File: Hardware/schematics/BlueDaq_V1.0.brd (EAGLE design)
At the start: 100 x 80 mm, 66 parts, among them IC1 MEGA8-AI, Q1 MMBT2222, Q2 MMBT2222, Q3 MMBT2222, Q4 MMBT2222, U1 MCP73831, U2 TPS61200, U3 BME280, U4 MIC5225-3.3, U5 MIC5219 5V, X1 USB-MICROB, X2 3.5mm, X4 3.5mm, Y1 16 mhz

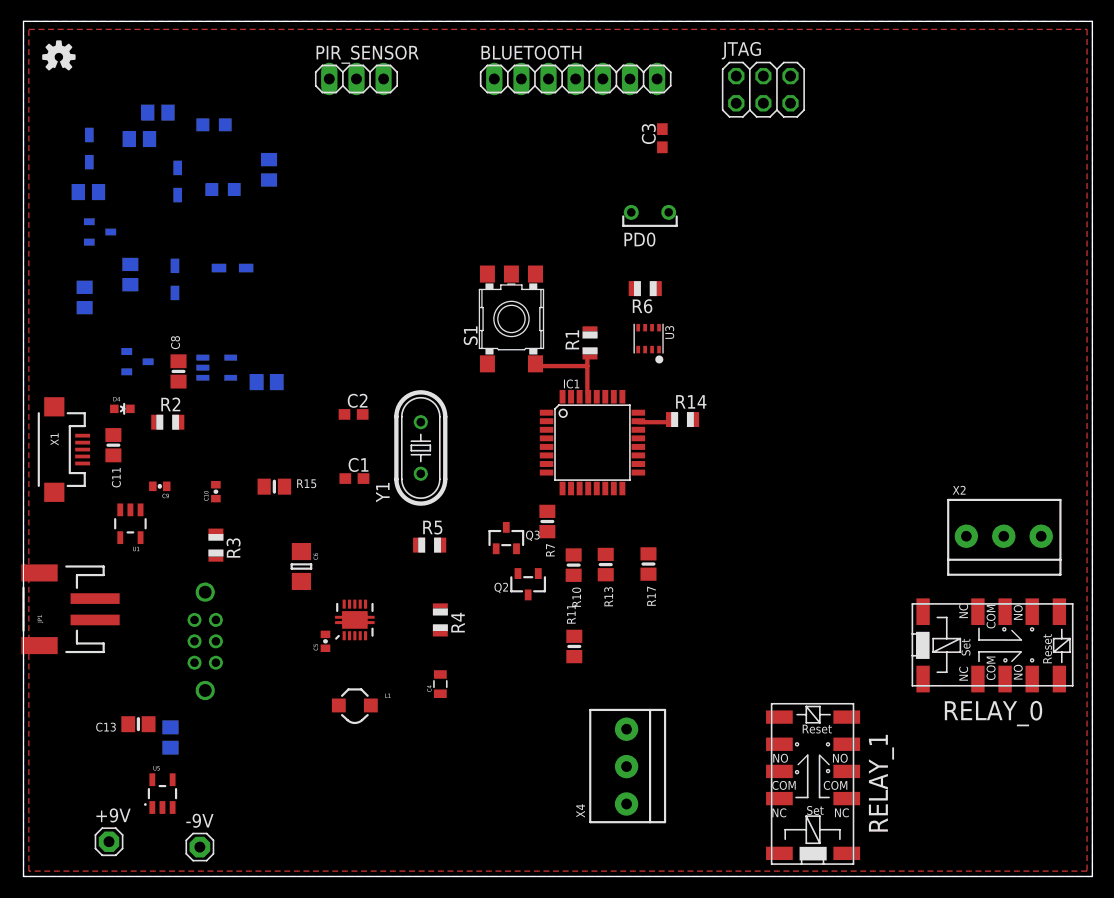
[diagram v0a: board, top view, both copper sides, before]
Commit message: updated board
updated layout. starting to have issue connecting gnd properly. added DRU/cam processor for OSH
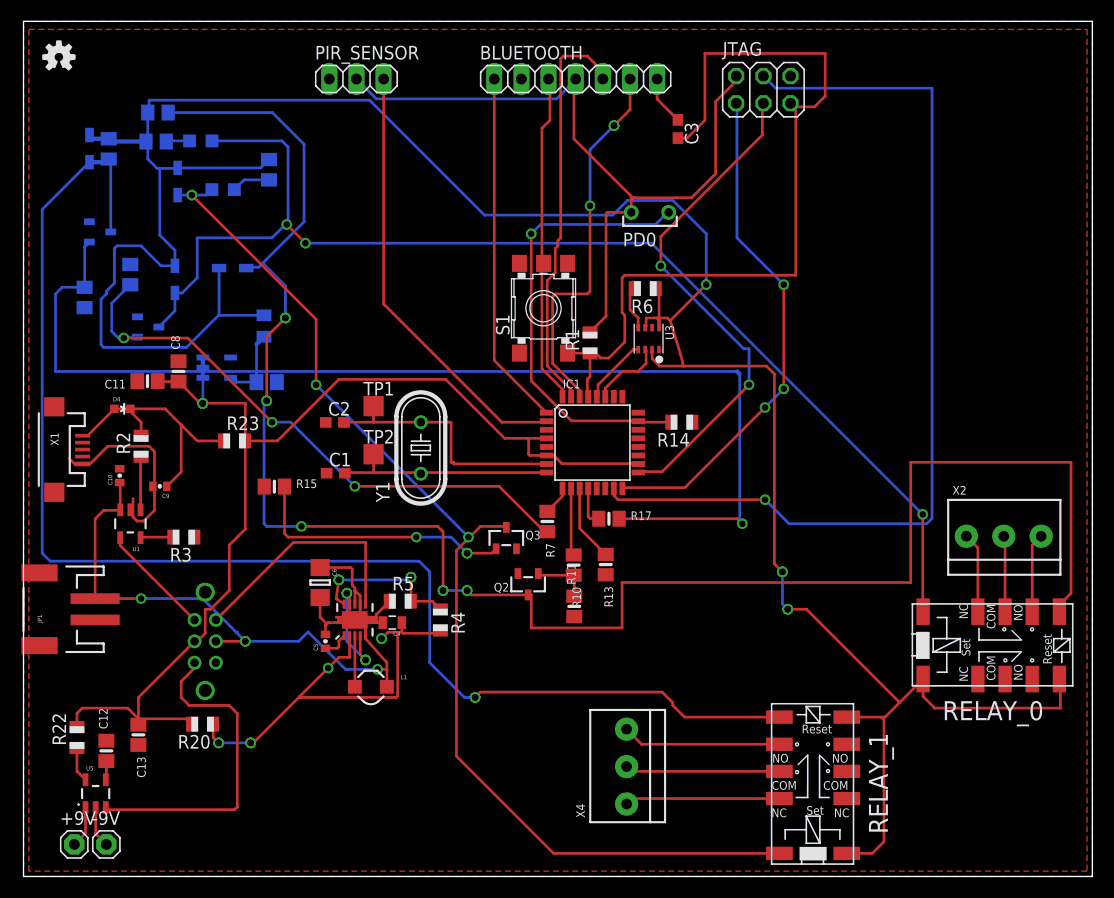
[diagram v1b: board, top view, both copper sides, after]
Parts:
- added R20, R21, R22, R23: 0, adafruit:R0805
- added TP1, TP2: TPTP19SQ, testpad:TP19SQ
- moved C10 9.12 mm to (9.00, 37.5)
- moved -9V 8.75 mm to (7.75, 3.00)
- moved C4 7.30 mm to (34.5, 23.8), turned to 180 degrees
- moved C11 6.79 mm to (11.6, 46.3), turned to 180 degrees
- moved U5 6.25 mm to (6.75, 7.75)
- moved C12 6.13 mm to (7.75, 11.8), flipped to the top
- moved R5 5.93 mm to (35.2, 25.8)
- moved R17 5.63 mm to (54.8, 33.5), turned to 0 degrees
- moved R19 4.46 mm to (7.97, 68.1), turned to 90 degrees
- moved R11 3.75 mm to (51.5, 25.3)
- moved Q1 3.40 mm to (11.7, 51.4)
- moved R2 3.36 mm to (11.0, 40.2), turned to 90 degrees
- moved +9V 3.26 mm to (4.75, 3.00)
- moved S1 3.16 mm to (48.6, 53.2)
- moved R3 3.09 mm to (15.0, 31.8), turned to 180 degrees
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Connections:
- new net N$20: C4.1, R20.1, R4.2, U2.2
- new net N$21: R22.1, U5.5
- new net N$23: C9.1, D4.A, R23.1, X1.VBUS
- new net OUT: C7.1, R21.1, U4.5
- net 3.3V: now also R21.2; no longer C7.1, U4.5
- net VCC: now also R20.2, R22.2, R23.2; no longer C4.1, C9.1, D4.A, R4.2, U2.2, U5.5, X1.VBUS
- net XTAL1: now also TP1.TP
- net XTAL2: now also TP2.TP
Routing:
- net 3.3V: track 0.00 -> 242.2 mm, vias 0 -> 3
- net VCC: track 0.00 -> 175.6 mm, vias 0 -> 2
- net N$25: track 0.00 -> 169.0 mm, vias 0 -> 5
- net N$12: track 0.00 -> 128.4 mm, vias 0 -> 1
- net N$6: track 0.00 -> 113.6 mm, vias 0 -> 3
- net N$7: track 0.00 -> 105.1 mm, vias 0 -> 3
- net N$13: track 0.00 -> 104.6 mm, vias 0 -> 1
- net SPI_MOSI: track 0.00 -> 88.2 mm, vias 0 -> 1
- net RESET_PIN: track 0.00 -> 77.7 mm
- net VBATT: track 0.00 -> 62.9 mm, vias 0 -> 3
- net N$22: track 0.00 -> 55.0 mm, vias 0 -> 3
- net SPI_SCK: track 0.00 -> 47.8 mm, vias 0 -> 2
- net SPI_MISO: track 0.00 -> 47.5 mm, vias 0 -> 3
- net N$1: track 0.00 -> 42.1 mm, vias 0 -> 1
- net N$20: track 0.00 -> 41.6 mm, vias 0 -> 4
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
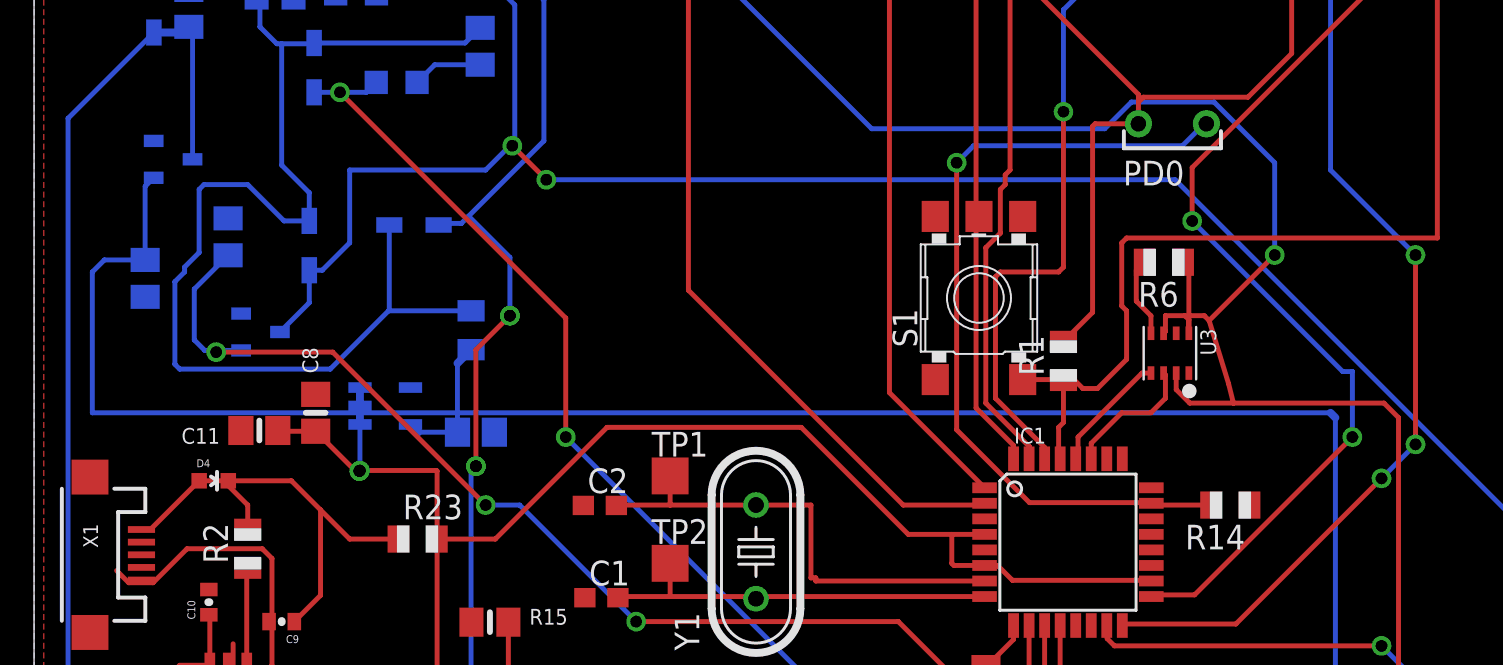
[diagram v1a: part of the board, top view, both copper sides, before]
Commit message: no more airwires, only need to clear DRC
everything is router now, for better or worse
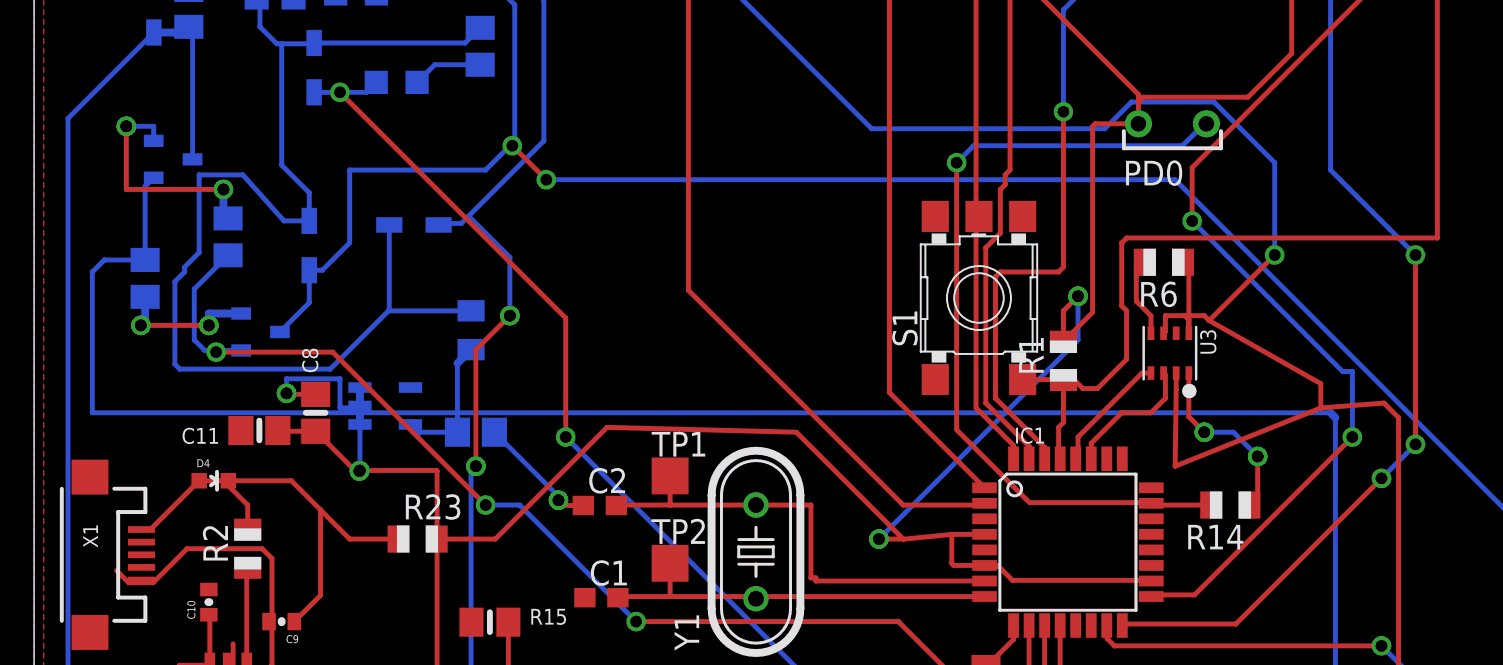
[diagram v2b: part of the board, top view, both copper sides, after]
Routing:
- net GND: track 19.0 -> 62.1 mm, vias 0 -> 8
- net VCC: track 175.6 -> 196.3 mm, vias 2 -> 4
- net 3.3V: track 242.2 -> 250.9 mm
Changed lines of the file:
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@@
 <?xml version="1.0" encoding="utf-8"?>
 <!DOCTYPE eagle SYSTEM "eagle.dtd">
-<eagle version="7.5.0">
+<eagle version="7.6.0">
 <drawing>
 <settings>
@@
 <wire x1="51.625" y1="74.5" x2="51.66" y2="74.61" width="0.254" layer="16"/>
 <wire x1="48.9374" y1="40.99" x2="47.25" y2="40.99" width="0.254" layer="1"/>
-<wire x1="47.25" y1="40.99" x2="45.01" y2="40.99" width="0.254" layer="1"/>
-<wire x1="45.01" y1="40.99" x2="39.5" y2="46.5" width="0.254" layer="1"/>
-<wire x1="39.5" y1="46.5" x2="29.5" y2="46.5" width="0.254" layer="1"/>
+<wire x1="47.25" y1="40.99" x2="44.76" y2="40.74" width="0.254" layer="1"/>
+<wire x1="44.75" y1="40.75" x2="39.25" y2="46.25" width="0.254" layer="1"/>
+<wire x1="39.25" y1="46.25" x2="29.5" y2="46.5" width="0.254" layer="1"/>
 <wire x1="29.5" y1="46.5" x2="23.75" y2="40.75" width="0.254" layer="1"/>
 <wire x1="23.75" y1="40.75" x2="20.75" y2="40.75" width="0.254" layer="1"/>
@@
 <wire x1="47.36" y1="39.39" x2="47.25" y2="39.5" width="0.254" layer="1"/>
 <wire x1="47.25" y1="39.5" x2="47.25" y2="40.99" width="0.254" layer="1"/>
-<wire x1="48.9374" y1="40.99" x2="53" y2="50.92" width="0" layer="19" extent="1-1"/>
+<wire x1="53" y1="50.92" x2="53" y2="52.5" width="0.254" layer="1"/>
+<wire x1="53" y1="52.5" x2="53.75" y2="53.25" width="0.254" layer="1"/>
+<via x="53.75" y="53.25" extent="1-16" drill="0.6"/>
+<wire x1="53.75" y1="53.25" x2="53.75" y2="51" width="0.254" layer="16"/>
+<wire x1="53.75" y1="51" x2="43.5" y2="40.75" width="0.254" layer="16"/>
+<via x="43.5" y="40.75" extent="1-16" drill="0.6"/>
+<wire x1="43.5" y1="40.75" x2="44.75" y2="40.75" width="0.254" layer="1"/>
+<wire x1="44.75" y1="40.75" x2="44.76" y2="40.74" width="0.254" layer="1"/>
 </signal>
 <signal name="GND">
@@
 <wire x1="9" y1="38.125" x2="9" y2="38.15" width="0.254" layer="1"/>
 <wire x1="9" y1="38.125" x2="9.00003125" y2="38.14998125" width="0.254" layer="1"/>
-<wire x1="14.5" y1="48.2" x2="16.7799" y2="47.6" width="0" layer="19" extent="1-16"/>
-<wire x1="9.99" y1="57.26" x2="6.16" y2="61.25" width="0" layer="19" extent="16-16"/>
-<wire x1="5.72" y1="53.22" x2="10.66" y2="52.36" width="0" layer="19" extent="16-16"/>
-<wire x1="28.28" y1="42.48" x2="23.7" y2="46.25" width="0" layer="19" extent="1-16"/>
-<wire x1="48.9374" y1="41.79" x2="46.4" y2="48.96" width="0" layer="19" extent="1-1"/>
-<wire x1="59.455" y1="49.295" x2="62.59" y2="42.5" width="0" layer="19" extent="1-1"/>
+<wire x1="9.99" y1="57.26" x2="9.75" y2="57.26" width="0.4064" layer="16"/>
+<wire x1="9.75" y1="57.26" x2="9.75" y2="58.75" width="0.4064" layer="16"/>
+<via x="9.75" y="58.75" extent="1-16" drill="0.6"/>
+<wire x1="9.75" y1="58.75" x2="4.75" y2="58.75" width="0.254" layer="1"/>
+<wire x1="4.75" y1="58.75" x2="4.75" y2="62" width="0.254" layer="1"/>
+<via x="4.75" y="62" extent="1-16" drill="0.6"/>
+<wire x1="4.75" y1="62" x2="6.16" y2="62" width="0.254" layer="16"/>
+<wire x1="6.16" y1="62" x2="6.16" y2="61.25" width="0.254" layer="16"/>
+<wire x1="10.66" y1="52.36" x2="9" y2="52.36" width="0.4064" layer="16"/>
+<wire x1="9" y1="52.36" x2="9" y2="51.75" width="0.4064" layer="16"/>
+<via x="9" y="51.75" extent="1-16" drill="0.6"/>
+<wire x1="9" y1="51.75" x2="5.5" y2="51.75" width="0.254" layer="1"/>
+<via x="5.5" y="51.75" extent="1-16" drill="0.6"/>
+<wire x1="5.5" y1="51.75" x2="5.72" y2="51.75" width="0.4064" layer="16"/>
+<wire x1="5.72" y1="51.75" x2="5.72" y2="53.22" width="0.4064" layer="16"/>
+<wire x1="14.5" y1="48.2" x2="13" y2="48.2" width="0.254" layer="1"/>
+<wire x1="13" y1="48.2" x2="13" y2="48.25" width="0.254" layer="1"/>
+<via x="13" y="48.25" extent="1-16" drill="0.6"/>
+<wire x1="13" y1="48.25" x2="13" y2="49" width="0.254" layer="16"/>
+<wire x1="13" y1="49" x2="15.75" y2="49" width="0.254" layer="16"/>
+<wire x1="15.75" y1="49" x2="15.75" y2="47.5" width="0.254" layer="16"/>
+<wire x1="15.75" y1="47.5" x2="16.7799" y2="47.5" width="0.254" layer="16"/>
+<wire x1="16.7799" y1="47.5" x2="16.7799" y2="47.6" width="0.254" layer="16"/>
+<wire x1="28.28" y1="42.48" x2="27" y2="42.48" width="0.254" layer="1"/>
+<wire x1="27" y1="42.48" x2="27" y2="42.75" width="0.254" layer="1"/>
+<via x="27" y="42.75" extent="1-16" drill="0.6"/>
+<wire x1="27" y1="42.75" x2="27" y2="42.95" width="0.254" layer="16"/>
+<wire x1="27" y1="42.95" x2="23.7" y2="46.25" width="0.254" layer="16"/>
+<wire x1="59.455" y1="49.295" x2="59.455" y2="47.045" width="0.254" layer="1"/>
+<wire x1="59.455" y1="47.045" x2="60.25" y2="46.25" width="0.254" layer="1"/>
+<via x="60.25" y="46.25" extent="1-16" drill="0.6"/>
+<wire x1="60.25" y1="46.25" x2="61.75" y2="46.25" width="0.254" layer="16"/>
+<wire x1="61.75" y1="46.25" x2="63" y2="45" width="0.254" layer="16"/>
+<via x="63" y="45" extent="1-16" drill="0.6"/>
+<wire x1="63" y1="45" x2="63" y2="42.91" width="0.254" layer="1"/>
+<wire x1="63" y1="42.91" x2="62.59" y2="42.5" width="0.254" layer="1"/>
 </signal>
 <signal name="BT_RX">
@@
 <wire x1="18.25" y1="52.5" x2="22.5" y2="52.5" width="0.254" layer="16"/>
 <wire x1="14.17" y1="57.13" x2="12.87" y2="57.13" width="0.254" layer="16"/>
-<wire x1="12.87" y1="57.13" x2="11" y2="59" width="0.254" layer="16"/>
-<wire x1="11" y1="59" x2="8.75" y2="59" width="0.254" layer="16"/>
-<wire x1="8.75" y1="59" x2="8.5" y2="58.75" width="0.254" layer="16"/>
-<wire x1="8.5" y1="58.75" x2="8.5" y2="55.5" width="0.254" layer="16"/>
+<wire x1="12.87" y1="57.13" x2="10.75" y2="59.5" width="0.254" layer="16"/>
+<wire x1="10.75" y1="59.5" x2="8.5" y2="59.5" width="0.254" layer="16"/>
+<wire x1="8.5" y1="59.5" x2="8.5" y2="55.5" width="0.254" layer="16"/>
 <wire x1="8.5" y1="55.5" x2="7.75" y2="54.75" width="0.254" layer="16"/>
 <wire x1="7.75" y1="54.75" x2="7.75" y2="54.5" width="0.254" layer="16"/>
@@
 <wire x1="58.25" y1="51.44" x2="58.155" y2="51.345" width="0.254" layer="1"/>
 <wire x1="58.805" y1="49.295" x2="58.805" y2="48.445" width="0.254" layer="1"/>
-<wire x1="58.805" y1="48.445" x2="59.5" y2="47.75" width="0.254" layer="1"/>
-<wire x1="59.5" y1="47.75" x2="61.75" y2="47.75" width="0.254" layer="1"/>
-<wire x1="61.75" y1="47.75" x2="61.5" y2="48.75" width="0.254" layer="1"/>
-<wire x1="61.5" y1="48.75" x2="60.5" y2="52" width="0.254" layer="1"/>
+<wire x1="58.805" y1="48.445" x2="58.75" y2="44.5" width="0.254" layer="1"/>
+<wire x1="58.75" y1="44.5" x2="66.25" y2="47.5" width="0.254" layer="1"/>
+<wire x1="66.25" y1="47.5" x2="66.25" y2="48.75" width="0.254" layer="1"/>
+<wire x1="66.25" y1="48.75" x2="60.5" y2="52" width="0.254" layer="1"/>
 <wire x1="60.5" y1="52" x2="60.25" y2="52.25" width="0.254" layer="1"/>
 <wire x1="60.25" y1="52.25" x2="59.455" y2="52.25" width="0.254" layer="1"/>
-<wire x1="61.75" y1="47.75" x2="69.5" y2="47.75" width="0.254" layer="1"/>
+<wire x1="66.25" y1="47.5" x2="69.5" y2="47.75" width="0.254" layer="1"/>
 <wire x1="69.5" y1="47.75" x2="70.25" y2="47" width="0.254" layer="1"/>
 <wire x1="70.25" y1="47" x2="70.25" y2="29.25" width="0.254" layer="1"/>
@@
 <via x="24.5" y="52.25" extent="1-16" drill="0.6"/>
 </signal>
+<signal name="N$40">
+<via x="9.75" y="58.75" extent="1-16" drill="0.6"/>
+</signal>
+<signal name="N$46">
+<via x="4.75" y="62" extent="1-16" drill="0.6"/>
+</signal>
+<signal name="N$48">
+<via x="5.5" y="51.75" extent="1-16" drill="0.6"/>
+</signal>
+<signal name="N$49">
+<via x="9" y="51.75" extent="1-16" drill="0.6"/>
+</signal>
+<signal name="N$50">
+<via x="13" y="48.25" extent="1-16" drill="0.6"/>
+</signal>
+<signal name="N$51">
+<via x="27" y="42.75" extent="1-16" drill="0.6"/>
+</signal>
+<signal name="N$52">
+<via x="53.75" y="53.25" extent="1-16" drill="0.6"/>
+</signal>
+<signal name="N$53">
+<via x="43.5" y="40.75" extent="1-16" drill="0.6"/>
+</signal>
+<signal name="N$54">
+<via x="60.25" y="46.25" extent="1-16" drill="0.6"/>
+</signal>
+<signal name="N$55">
+<via x="63" y="45" extent="1-16" drill="0.6"/>
+</signal>
 </signals>
